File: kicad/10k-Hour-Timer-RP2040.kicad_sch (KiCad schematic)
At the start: 13 parts, among them J1 JST_SH_SM03B, J2 USB_C_Receptacle_USB2.0_16P, J8 Conn_01x03_Pin, U1 USBLC6-2SC6

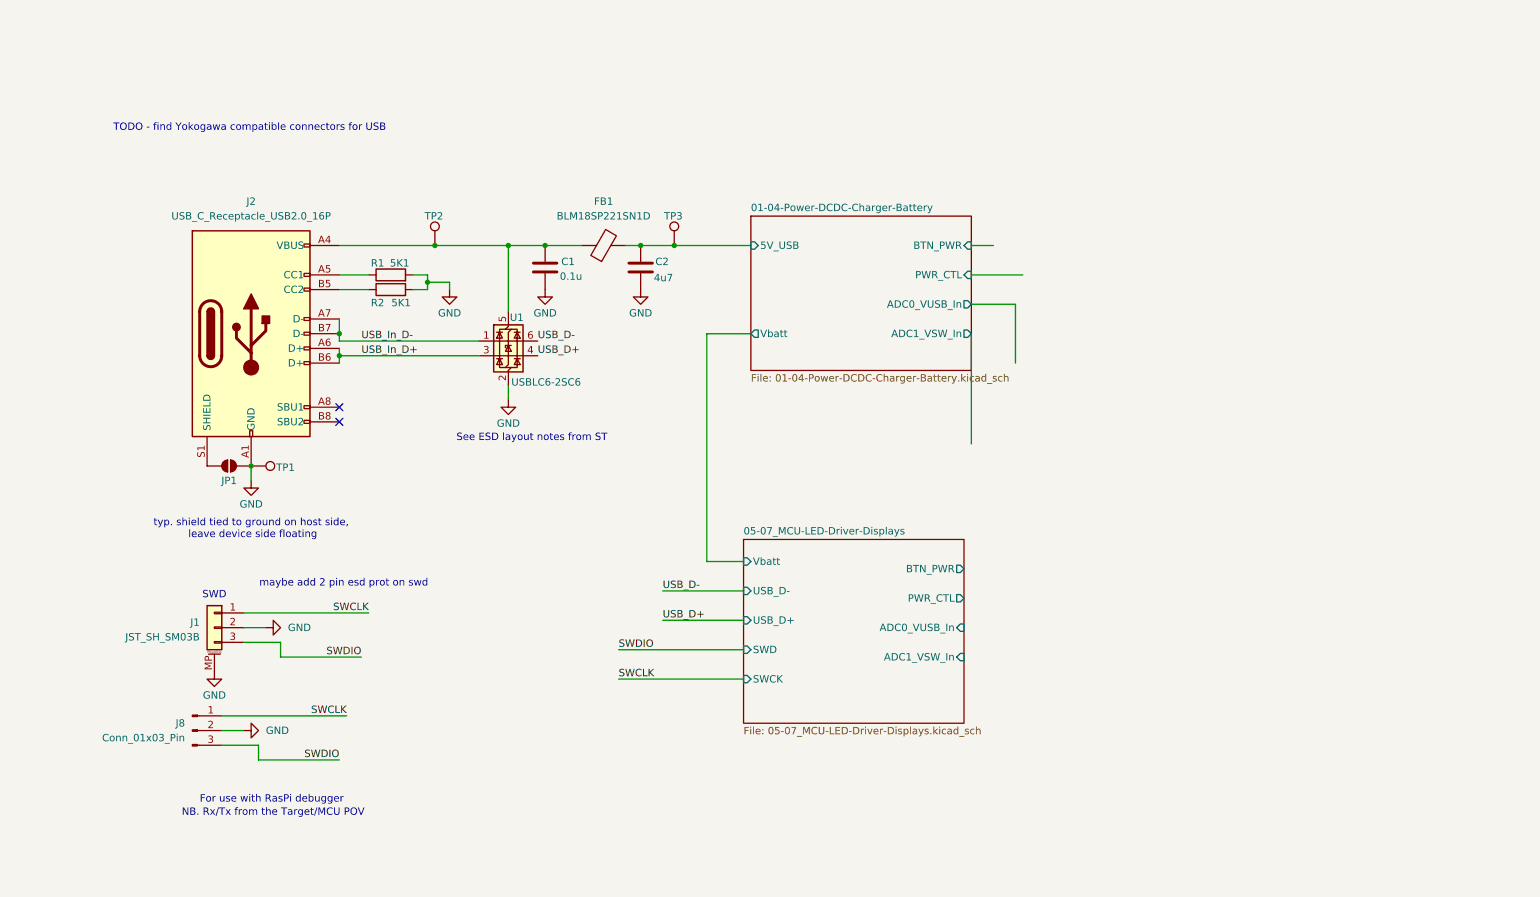
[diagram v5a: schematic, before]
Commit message: rtc new sheet, pullups
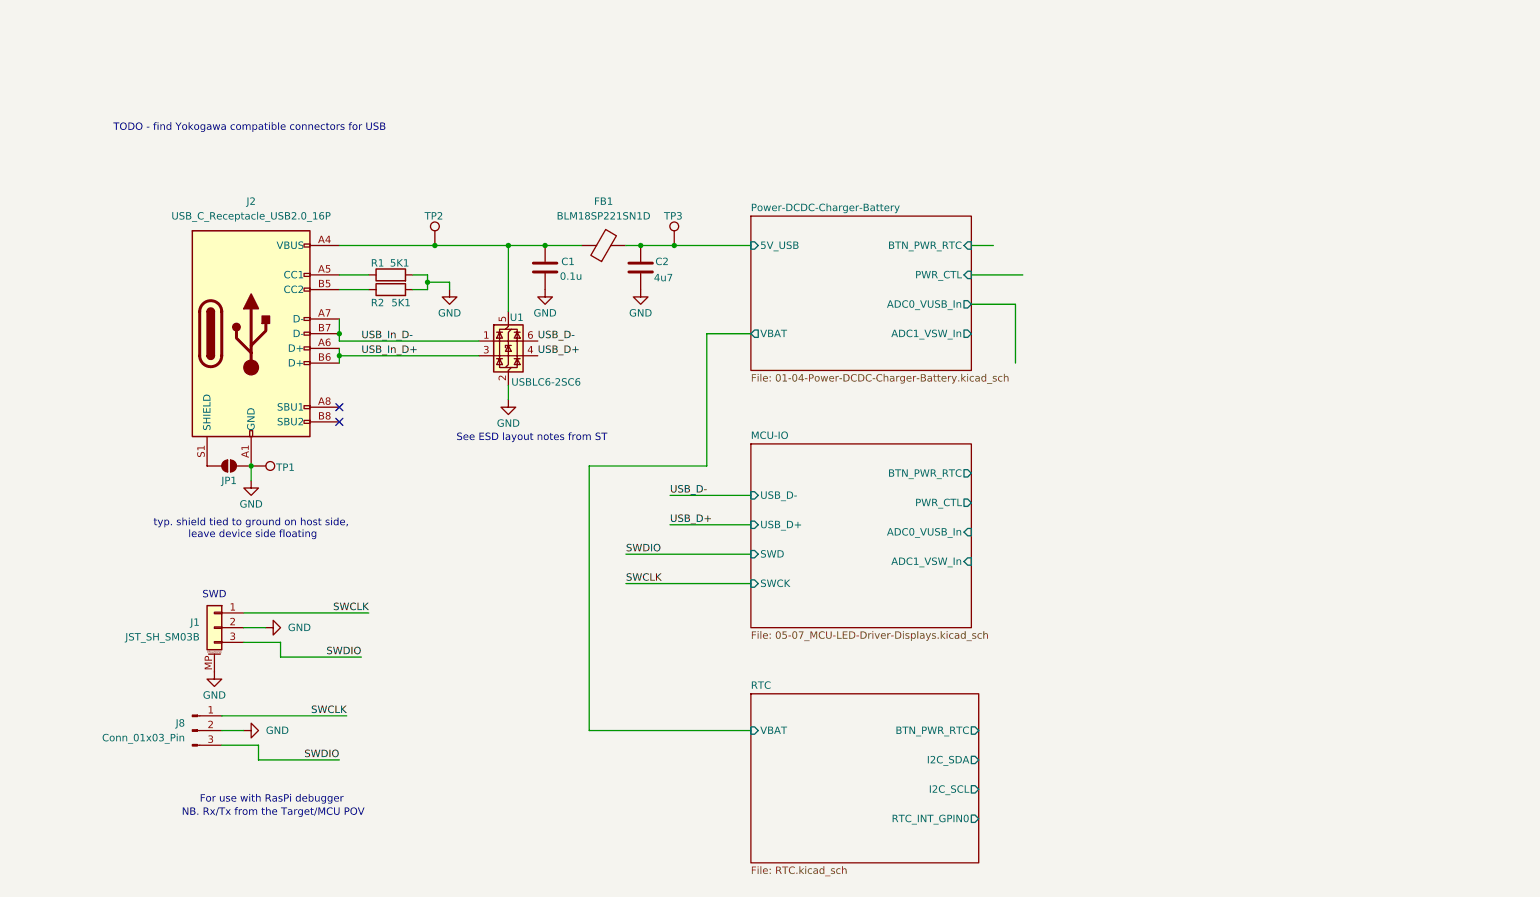
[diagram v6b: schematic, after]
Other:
- sheet 01-04-Power-DCDC-Charger-Battery renamed Power-DCDC-Charger-Battery
- sheet 05-07_MCU-LED-Driver-Displays renamed MCU-IO
- added sheet RTC (RTC.kicad_sch)
- sheet MCU-IO ports: added BTN_PWR_RTC; removed BTN_PWR, Vbatt
- sheet Power-DCDC-Charger-Battery ports: added BTN_PWR_RTC, VBAT; removed BTN_PWR, Vbatt
- note removed: "maybe add 2 pin esd prot on swd"
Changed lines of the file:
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@@
-		)
-	)
-	(text "maybe add 2 pin esd prot on swd"
-		(exclude_from_sim no)
-		(at 74.422 115.57 0)
-		(effects
-			(font
-				(size 1.27 1.27)
-			)
 		)
 	)
@@
 	(wire
 		(pts
+			(xy 116.84 140.97) (xy 144.78 140.97)
+		)
+		(stroke
+			(width 0)
+			(type default)
+		)
+	)
+	(wire
+		(pts
 			(xy 144.78 72.39) (xy 137.16 72.39)
 		)
@@
 	(wire
 		(pts
-			(xy 137.16 111.76) (xy 143.51 111.76)
+			(xy 137.16 95.25) (xy 116.84 95.25)
 		)
 		(stroke
@@
 	(wire
 		(pts
+			(xy 116.84 95.25) (xy 116.84 140.97)
+		)
+		(stroke
+			(width 0)
+			(type default)
+		)
+	)
+	(wire
+		(pts
 			(xy 63.5 128.27) (xy 77.47 128.27)
 		)
@@
 	(wire
 		(pts
-			(xy 121.92 132.08) (xy 143.51 132.08)
+			(xy 123.19 115.57) (xy 144.78 115.57)
 		)
 		(stroke
@@
 	(wire
 		(pts
-			(xy 182.88 72.39) (xy 182.88 91.44)
-		)
-		(stroke
-			(width 0)
-			(type default)
-		)
-	)
-	(wire
-		(pts
 			(xy 57.15 120.65) (xy 78.74 120.65)
 		)
@@
 	(wire
 		(pts
-			(xy 121.92 127) (xy 143.51 127)
+			(xy 123.19 110.49) (xy 144.78 110.49)
 		)
 		(stroke
@@
 	(wire
 		(pts
-			(xy 129.54 116.84) (xy 143.51 116.84)
+			(xy 130.81 100.33) (xy 144.78 100.33)
+		)
+		(stroke
+			(width 0)
+			(type default)
+		)
+	)
+	(wire
+		(pts
+			(xy 137.16 72.39) (xy 137.16 95.25)
 		)
 		(stroke
@@
 	(wire
 		(pts
-			(xy 137.16 72.39) (xy 137.16 111.76)
-		)
-		(stroke
-			(width 0)
-			(type default)
-		)
-	)
-	(wire
-		(pts
 			(xy 53.34 138.43) (xy 74.93 138.43)
 		)
@@
 	(wire
 		(pts
-			(xy 129.54 121.92) (xy 143.51 121.92)
+			(xy 130.81 105.41) (xy 144.78 105.41)
 		)
 		(stroke
@@
 	)
 	(label "SWCLK"
-		(at 121.92 132.08 0)
+		(at 123.19 115.57 0)
 		(effects
 			(font
@@
 	)
 	(label "USB_D+"
-		(at 129.54 121.92 0)
+		(at 130.81 105.41 0)
 		(effects
 			(font
@@
 	)
 	(label "SWDIO"
-		(at 121.92 127 0)
+		(at 123.19 110.49 0)
 		(effects
 			(font
@@
 	)
 	(label "USB_D-"
-		(at 129.54 116.84 0)
+		(at 130.81 100.33 0)
 		(effects
 			(font
@@
 	)
 	(sheet
-		(at 143.51 107.95)
+		(at 144.78 134.62)
+		(size 39.37 29.21)
+		(exclude_from_sim no)
+		(in_bom yes)
+		(on_board yes)
+		(dnp no)
+		(fields_autoplaced yes)
+		(stroke
+			(width 0.1524)
+			(type solid)
+		)
+		(fill
+			(color 0 0 0 0.0000)
+		)
+		(property "Sheetname" "RTC"
+			(at 144.78 133.9084 0)
+			(effects
+				(font
+					(size 1.27 1.27)
+				)
+				(justify left bottom)
+			)
+		)
+		(property "Sheetfile" "RTC.kicad_sch"
+			(at 144.78 164.4146 0)
+			(effects
+				(font
+					(size 1.27 1.27)
+				)
+				(justify left top)
+			)
+		)
+		(pin "BTN_PWR_RTC" output
+			(at 184.15 140.97 0)
+			(effects
+				(font
+					(size 1.27 1.27)
+				)
+				(justify right)
+			)
+		)
+		(pin "I2C_SDA" output
+			(at 184.15 146.05 0)
+			(effects
+				(font
+					(size 1.27 1.27)
+				)
+				(justify right)
+			)
+		)
+		(pin "I2C_SCL" output
+			(at 184.15 151.13 0)
+			(effects
+				(font
+					(size 1.27 1.27)
+				)
+				(justify right)
+			)
+		)
+		(pin "RTC_INT_GPIN0" output
+			(at 184.15 156.21 0)
+			(effects
+				(font
+					(size 1.27 1.27)
+				)
+				(justify right)
+			)
+		)
+		(pin "VBAT" input
+			(at 144.78 140.97 180)
+			(effects
+				(font
+					(size 1.27 1.27)
+				)
+				(justify left)
+			)
+		)
+		(instances
+			(project "10k-Hour-Timer-RP2040"
+				(path "/9d26b66f-2a94-42e5-8460-016e0bf95186"
+					(page "4")
+				)
+			)
+		)
+	)
+	(sheet
+		(at 144.78 91.44)
 		(size 38.1 31.75)
 		(exclude_from_sim no)
@@
 			(color 0 0 0 0.0000)
 		)
-		(property "Sheetname" "05-07_MCU-LED-Driver-Displays"
-			(at 143.51 107.2384 0)
+		(property "Sheetname" "MCU-IO"
+			(at 144.78 90.7284 0)
 			(effects
 				(font
@@
 		)
 		(property "Sheetfile" "05-07_MCU-LED-Driver-Displays.kicad_sch"
-			(at 143.51 140.2846 0)
+			(at 144.78 123.7746 0)
 			(effects
 				(font
@@
 		)
 		(pin "USB_D+" input
-			(at 143.51 121.92 180)
+			(at 144.78 105.41 180)
 			(effects
 				(font
@@
 		)
 		(pin "USB_D-" input
-			(at 143.51 116.84 180)
+			(at 144.78 100.33 180)
 			(effects
 				(font
@@
 		)
 		(pin "SWD" input
-			(at 143.51 127 180)
+			(at 144.78 110.49 180)
 			(effects
 				(font
@@
 		)
 		(pin "SWCK" input
-			(at 143.51 132.08 180)
+			(at 144.78 115.57 180)
 			(effects
 				(font
@@
 			)
 		)
-		(pin "BTN_PWR" output
-			(at 181.61 113.03 0)
+		(pin "BTN_PWR_RTC" output
+			(at 182.88 96.52 0)
 			(effects
 				(font
@@
 		)
 		(pin "PWR_CTL" output
-			(at 181.61 118.11 0)
+			(at 182.88 101.6 0)
 			(effects
 				(font
@@
 		)
 		(pin "ADC0_VUSB_In" input
-			(at 181.61 123.19 0)
+			(at 182.88 106.68 0)
 			(effects
 				(font
@@
 		)
 		(pin "ADC1_VSW_In" input
-			(at 181.61 128.27 0)
+			(at 182.88 111.76 0)
 			(effects
 				(font
@@
 				)
 				(justify right)
-			)
-		)
-		(pin "Vbatt" input
-			(at 143.51 111.76 180)
-			(effects
-				(font
-					(size 1.27 1.27)
-				)
-				(justify left)
 			)
 		)
@@
 			(color 0 0 0 0.0000)
 		)
-		(property "Sheetname" "01-04-Power-DCDC-Charger-Battery"
+		(property "Sheetname" "Power-DCDC-Charger-Battery"
 			(at 144.78 51.3584 0)
 			(effects
@@
 			)
 		)
-		(pin "BTN_PWR" input
+		(pin "BTN_PWR_RTC" input
 			(at 182.88 57.15 0)
 			(effects
@@
 			)
 		)
-		(pin "Vbatt" output
+		(pin "VBAT" output
 			(at 144.78 72.39 180)
 			(effects

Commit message: pre ERC
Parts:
- added BOM1: JST PH 2.0mm Connector Kit, symbol Project_Library:BOM_PLACEHOLDER
- added BOM2: Crimp Pliers for JST-PH connectors, symbol Project_Library:BOM_PLACEHOLDER
- C1, C2: footprint (none) -> Capacitor_SMD:C_0805_2012Metric_Pad1.18x1.45mm_HandSolder; MPN (none) -> (Generic); Manufacturer (none) -> (Generic); Package (none) -> 0805; Subsystem (none) -> 01A-USB; Supplier 1 (none) -> (Generic)
- FB1, JP1, U1: Subsystem (none) -> 01A-USB
- J3: renamed from J2; Subsystem (none) -> 01A-USB
- R1, R2: Manufacturer (none) -> (Generic); Package (none) -> 0805; Subsystem (none) -> 01A-USB; Supplier 1 (none) -> (Generic)
- TP1: value TestPoint -> GND; Subsystem (none) -> 01A-USB
- TP2: value TestPoint -> VBUS_IN; Subsystem (none) -> 01A-USB
- TP3: value TestPoint -> VBUS; Subsystem (none) -> 01A-USB
- renumbered J8 to J1, J1 to J2
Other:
- note added: "Non Mounted BOM Parts:"

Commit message: ERC done
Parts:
- C1: value 0.1u -> 10n; footprint Capacitor_SMD:C_0805_2012Metric_Pad1.18x1.45mm_HandSolder -> Capacitor_SMD:C_0603_1608Metric_Pad1.08x0.95mm_HandSolder; Package 0805 -> 0603
- C2: value 4u7 -> 100n; footprint Capacitor_SMD:C_0805_2012Metric_Pad1.18x1.45mm_HandSolder -> Capacitor_SMD:C_0603_1608Metric_Pad1.08x0.95mm_HandSolder; Package 0805 -> 0603
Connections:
- net GND: no longer J2.MP (MountPin)
- no-connect marks 2 -> 3
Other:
- sheet MCU-IO ports: added I2C_SCL, I2C_SDA, RTC_INT_GPIN0; removed none
- moved on the sheet: TP3
